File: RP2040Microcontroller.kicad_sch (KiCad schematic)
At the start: 128 parts, among them J2 Conn_01x02, J34 DIN-5_180degree, J36 USB_B, SW51 SW_Push, SW52 SW_Push, SW53 SW_Push, SW54 SW_Push, SW55 SW_Push, SW56 SW_Push, SW57 SW_Push, SW58 SW_Push, U1 NCP1117-3.3_SOT223, U2 W25Q128JVS, U3 RP2040, U39 CD74HC4067SM, U40 6N138, U43 TL074, U45 REF3012, U46 MCP4728, U47 TL074, U49 MCP23017_SS, Y1 ABLS-12.000MHZ-B4-T

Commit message: more work...
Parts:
- added J2: Conn_01x02, Connector_PinHeader_2.54mm:PinHeader_1x02_P2.54mm_Vertical, symbol Connector_Generic:Conn_01x02
- C1, C17, C4: value 10u -> 10uF
- C10, C8: value 1u -> 1uF; footprint Capacitor_SMD:C_0402_1005Metric -> Capacitor_SMD:C_0805_2012Metric
- C11, C12, C13, C14, C15, C16, C5, C6, C7, C9: value 100n -> 100nF; footprint Capacitor_SMD:C_0402_1005Metric -> Capacitor_SMD:C_0603_1608Metric
- C2, C3: value 27p -> 27pF; footprint Capacitor_SMD:C_0402_1005Metric -> Capacitor_SMD:C_0603_1608Metric
- C45: footprint Capacitor_SMD:C_0805_2012Metric_Pad1.18x1.45mm_HandSolder -> Capacitor_SMD:C_0603_1608Metric
- J34: value DIN-5_180degree -> DIN-504D-M5; footprint (none) -> SynthProjConnectors:SD-50BV
- J36: footprint (none) -> Connector_USB:USB_B_Lumberg_2411_02_Horizontal
- R1, R3, R4, R5: footprint Capacitor_SMD:C_0402_1005Metric -> Resistor_SMD:R_0603_1608Metric
- R? (x37): footprint Resistor_SMD:R_0805_2012Metric -> Resistor_SMD:R_0603_1608Metric
- R? (x17): footprint Resistor_SMD:R_0805_2012Metric_Pad1.20x1.40mm_HandSolder -> Resistor_SMD:R_0603_1608Metric
- U40: footprint (none) -> Package_SO:SOP-8_6.605x9.655mm_P2.54mm
- U43, U47: footprint (none) -> Package_SO:SO-14_3.9x8.65mm_P1.27mm
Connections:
- net GPIO0: now also J2.1 (Pin_1)
- net GPIO1: now also J2.2 (Pin_2)
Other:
- note added: "Debug"
- note added: "Voltage References"
- moved on the sheet: C2, C3, R5, R?, U43E, U45, Y1

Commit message: finishing schematic 1.0
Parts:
- added TP? (x6): TestPoint, TestPoint:TestPoint_Pad_D1.0mm, symbol Connector:TestPoint
- SW51, SW52, SW53, SW54, SW55, SW56, SW57, SW58: footprint (none) -> Button_Switch_THT:SW_PUSH_6mm_H13mm
- renumbered C15 to C?, C11 to C?, C13 to C?, C16 to C?, C14 to C?, C4 to C?, C2 to C?, C45 to C?, C3 to C?, C8 to C?, C7 to C?, C12 to C?, C9 to C?, C17 to C?, C6 to C?, C10 to C?, C1 to C?, C5 to C?, D10 to D?, J34 to J41, J36 to J42, J2 to J?, R2 to R?, R1 to R?, R3 to R?, R5 to R?, R4 to R?, RV39 to RV?, U49 to U44, U43 to U47, U47 to U49, U43 to U49, U2 to U?, U39 to U?, U3 to U?, U1 to U?, Y1 to Y?
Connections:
- net GPIO29_ADC0: now also TP?.1
- net VIN_A: now also TP?.1
- net VOUT_A: now also TP?.1
- net VREF1.0: now also TP?.1
- net VREF1.25: now also TP?.1
- net at C?.2, U46.6 (VOUTA): now also TP?.1
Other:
- moved on the sheet: C?, D?, J41, J42, J?, R?, RV?, SW51, SW52, SW53, SW54, SW55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

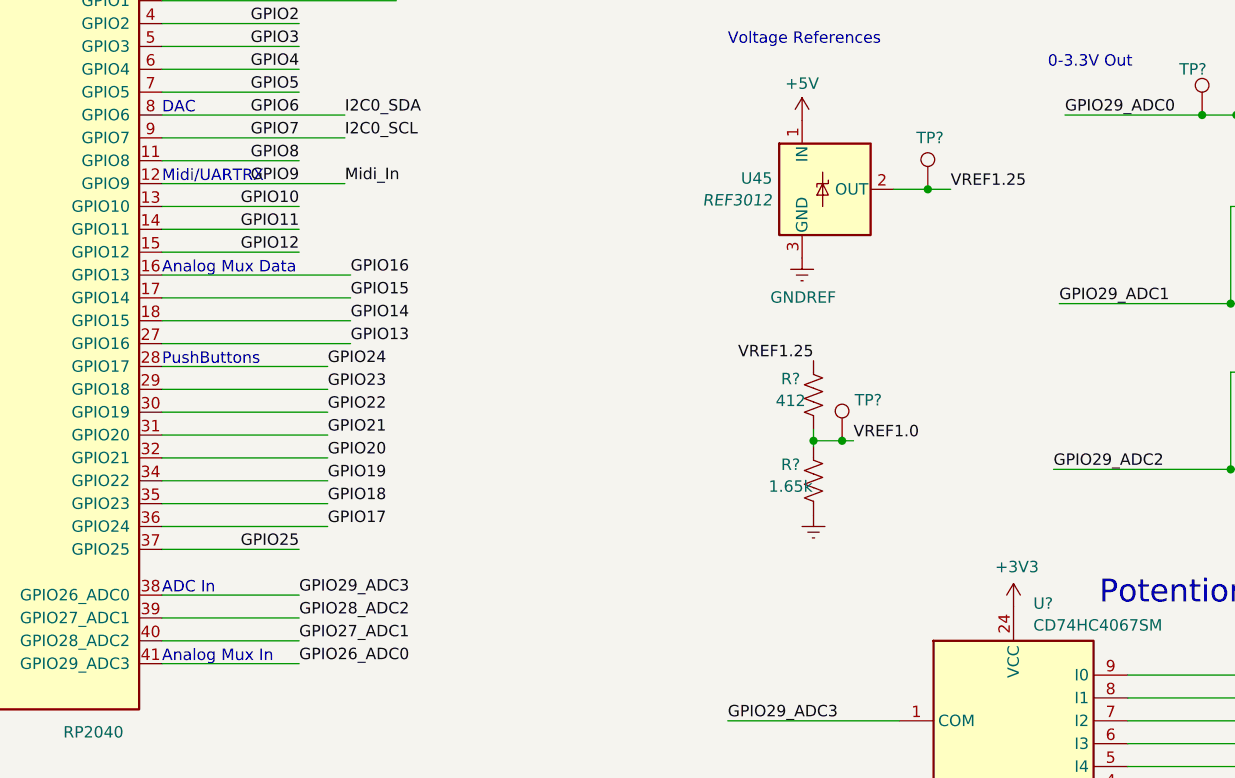
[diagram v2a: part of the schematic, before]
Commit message: doing some routing - split sequencer into another project
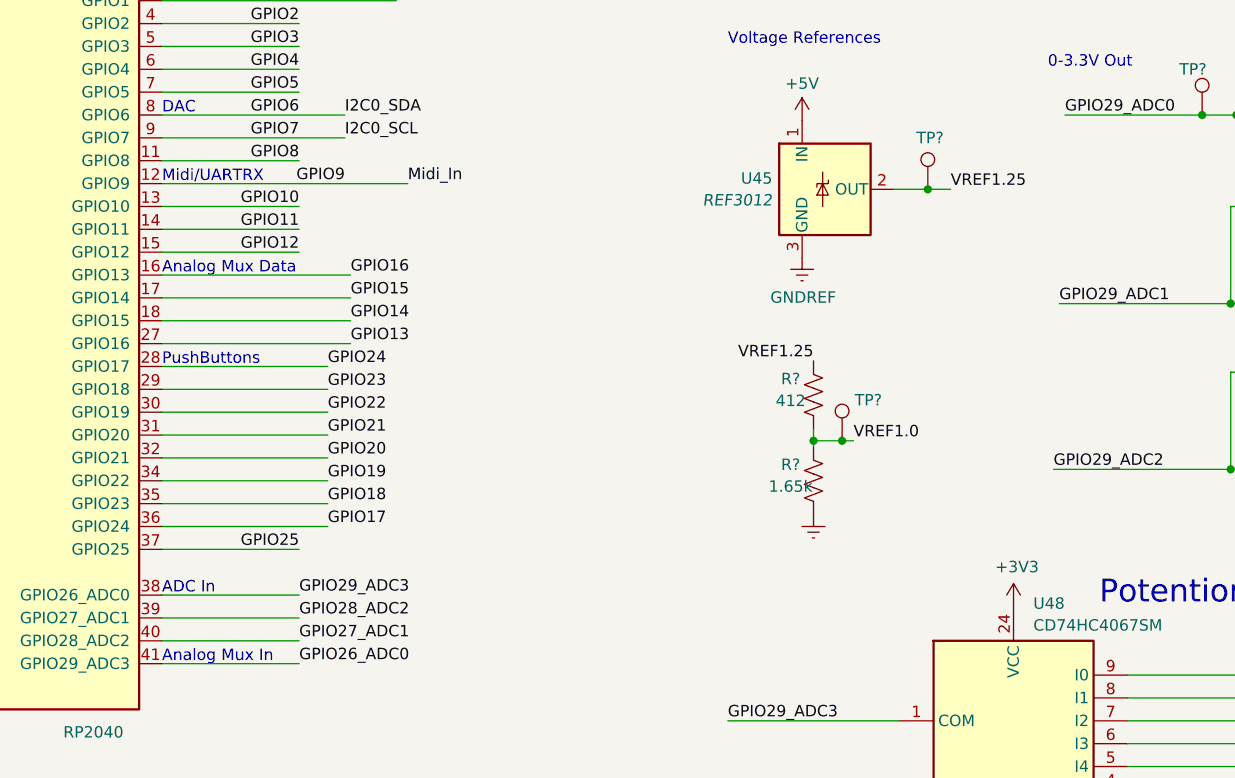
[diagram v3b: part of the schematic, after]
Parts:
- gave numbers to parts that had none: 1

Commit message: routing work...
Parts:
- removed R?: 28.7k, Resistor_SMD:R_0603_1608Metric, symbol Device:R_US
- removed R?: 10k, Resistor_SMD:R_0603_1608Metric, symbol Device:R_US
- removed R?: 66.5k, Resistor_SMD:R_0603_1608Metric, symbol Device:R_US
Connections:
- net VREF1.0: no longer U49.12 (+)
- net at U49.14: no longer U48.9 (I0)
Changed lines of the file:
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@@
 (kicad_sch (version 20230121) (generator eeschema)
   (paper "A3")
-  (junction (at 386.08 170.815) (diameter 0) (color 0 0 0 0)
-  )
   (junction (at 271.145 254) (diameter 0) (color 0 0 0 0)
   )
   (junction (at 88.9 94.615) (diameter 0) (color 0 0 0 0)
   )
-  (junction (at 368.3 181.61) (diameter 0) (color 0 0 0 0)
-  )
   (junction (at 207.645 73.66) (diameter 0) (color 0 0 0 0)
   )
@@
   (junction (at 368.3 41.275) (diameter 0) (color 0 0 0 0)
   )
-  (junction (at 386.08 179.07) (diameter 0) (color 0 0 0 0)
-  )
   (junction (at 271.145 231.14) (diameter 0) (color 0 0 0 0)
   )
@@
     (stroke (width 0) (type default))
   )
-  (wire (pts (xy 386.08 179.07) (xy 384.81 179.07))
-    (stroke (width 0) (type default))
-  )
   (wire (pts (xy 153.67 229.87) (xy 156.845 229.87))
     (stroke (width 0) (type default))
@@
     (stroke (width 0) (type default))
   )
-  (wire (pts (xy 386.08 170.815) (xy 378.46 170.815))
-    (stroke (width 0) (type default))
-  )
   (wire (pts (xy 351.79 212.09) (xy 377.19 212.09))
     (stroke (width 0) (type default))
@@
     (stroke (width 0) (type default))
   )
-  (wire (pts (xy 396.875 184.15) (xy 384.81 184.15))
-    (stroke (width 0) (type default))
-  )
   (wire (pts (xy 273.685 54.61) (xy 273.685 53.34))
     (stroke (width 0) (type default))
@@
     (stroke (width 0) (type default))
   )
-  (wire (pts (xy 397.51 179.07) (xy 396.875 179.07))
-    (stroke (width 0) (type default))
-  )
   (wire (pts (xy 342.265 119.38) (xy 343.535 119.38))
     (stroke (width 0) (type default))
@@
     (stroke (width 0) (type default))
   )
-  (wire (pts (xy 330.2 181.61) (xy 368.3 181.61))
-    (stroke (width 0) (type default))
-  )
   (wire (pts (xy 182.245 86.36) (xy 182.245 73.66))
     (stroke (width 0) (type default))
@@
     (stroke (width 0) (type default))
   )
-  (wire (pts (xy 389.255 179.07) (xy 386.08 179.07))
-    (stroke (width 0) (type default))
-  )
   (wire (pts (xy 321.945 158.75) (xy 341.63 158.75))
     (stroke (width 0) (type default))
@@
     (stroke (width 0) (type default))
   )
-  (wire (pts (xy 368.3 181.61) (xy 369.57 181.61))
-    (stroke (width 0) (type default))
-  )
   (wire (pts (xy 170.815 73.66) (xy 170.815 86.36))
     (stroke (width 0) (type default))
@@
     (stroke (width 0) (type default))
   )
-  (wire (pts (xy 368.3 170.815) (xy 368.3 181.61))
-    (stroke (width 0) (type default))
-  )
   (wire (pts (xy 67.31 209.55) (xy 67.31 214.63))
     (stroke (width 0) (type default))
@@
     (stroke (width 0) (type default))
   )
-  (wire (pts (xy 386.08 179.07) (xy 386.08 170.815))
-    (stroke (width 0) (type default))
-  )
   (wire (pts (xy 295.275 155.575) (xy 298.45 155.575))
     (stroke (width 0) (type default))
@@
     (stroke (width 0) (type default))
   )
-  (wire (pts (xy 370.84 170.815) (xy 368.3 170.815))
-    (stroke (width 0) (type default))
-  )
   (wire (pts (xy 159.385 171.45) (xy 145.415 171.45))
     (stroke (width 0) (type default))
@@
     (stroke (width 0) (type default))
   )
-  (wire (pts (xy 389.89 170.815) (xy 386.08 170.815))
-    (stroke (width 0) (type default))
-  )
   (wire (pts (xy 307.975 127.635) (xy 310.515 127.635))
     (stroke (width 0) (type default))
@@
     (effects (font (size 1.27 1.27)) (justify left bottom))
   )
-  (label "VREF1.0" (at 396.875 184.15 0) (fields_autoplaced)
-    (effects (font (size 1.27 1.27)) (justify left bottom))
-  )
   (label "QSPI_SD1" (at 118.11 114.935 180) (fields_autoplaced)
     (effects (font (size 1.27 1.27)) (justify right bottom))
@@
     (effects (font (size 1.27 1.27)) (justify left))
   )
-  (hierarchical_label "VIN_D" (shape input) (at 397.51 179.07 0) (fields_autoplaced)
-    (effects (font (size 1.27 1.27)) (justify left))
-  )
   (hierarchical_label "VIN_C" (shape input) (at 374.65 156.21 0) (fields_autoplaced)
     (effects (font (size 1.27 1.27)) (justify left))
@@
     )
   )
-  (symbol (lib_id "power:GNDREF") (at 397.51 170.815 0) (mirror y) (unit 1)
-    (in_bom yes) (on_board yes) (dnp no)
-    (property "Reference" "#PWR?" (at 397.51 177.165 0)
-      (effects (font (size 1.27 1.27)) hide)
-    )
-    (property "Value" "GNDREF" (at 397.383 175.2092 0)
-      (effects (font (size 1.27 1.27)) hide)
-    )
-    (property "Footprint" "" (at 397.51 170.815 0)
-      (effects (font (size 1.27 1.27)) hide)
-    )
-    (property "Datasheet" "" (at 397.51 170.815 0)
-      (effects (font (size 1.27 1.27)) hide)
-    )
-    (pin "1")
-    (instances
-      (project "SynthProj"
-        (path "/9021c97e-351f-4ed9-b393-50257df6a463/00000000-0000-0000-0000-0000659d0967"
-          (reference "#PWR?") (unit 1)
-        )
-        (path "/9021c97e-351f-4ed9-b393-50257df6a463/00000000-0000-0000-0000-0000659a4e2e"
-          (reference "#PWR?") (unit 1)
-        )
-        (path "/9021c97e-351f-4ed9-b393-50257df6a463/2f8f79cd-08c7-4a3d-ab4d-798613b0e4e6"
-          (reference "#PWR0524") (unit 1)
-        )
-      )
-    )
-  )
   (symbol (lib_id "Device:R_US") (at 367.03 129.54 90) (unit 1)
     (in_bom yes) (on_board yes) (dnp no)
@@
     )
   )
-  (symbol (lib_id "Device:R_US") (at 393.7 170.815 90) (unit 1)
-    (in_bom yes) (on_board yes) (dnp no)
-    (property "Reference" "R?" (at 393.7 168.275 90)
-      (effects (font (size 1.27 1.27)))
-    )
-    (property "Value" "28.7k" (at 393.7 165.735 90)
-      (effects (font (size 1.27 1.27)))
-    )
-    (property "Footprint" "Resistor_SMD:R_0603_1608Metric" (at 393.954 169.799 90)
-      (effects (font (size 1.27 1.27)) hide)
-    )
-    (property "Datasheet" "~" (at 393.7 170.815 0)
-      (effects (font (size 1.27 1.27)) hide)
-    )
-    (pin "2")
-    (pin "1")
-    (instances
-      (project "SynthProj"
-        (path "/9021c97e-351f-4ed9-b393-50257df6a463/00000000-0000-0000-0000-0000659d0967"
-          (reference "R?") (unit 1)
-        )
-        (path "/9021c97e-351f-4ed9-b393-50257df6a463/00000000-0000-0000-0000-0000659a4e2e"
-          (reference "R?") (unit 1)
-        )
-        (path "/9021c97e-351f-4ed9-b393-50257df6a463/0e948a88-c071-4754-aa3e-af223f738530"
-          (reference "R?") (unit 1)
-        )
-        (path "/9021c97e-351f-4ed9-b393-50257df6a463/2f8f79cd-08c7-4a3d-ab4d-798613b0e4e6"
-          (reference "R404") (unit 1)
-        )
-      )
-    )
-  )
   (symbol (lib_id "power:+3V3") (at 373.38 200.66 90) (unit 1)
     (in_bom yes) (on_board yes) (dnp no)
@@
     )
   )
-  (symbol (lib_id "Device:R_US") (at 374.65 170.815 90) (unit 1)
-    (in_bom yes) (on_board yes) (dnp no)
-    (property "Reference" "R?" (at 370.84 169.545 90)
-      (effects (font (size 1.27 1.27)))
-    )
-    (property "Value" "10k" (at 370.84 172.085 90)
-      (effects (font (size 1.27 1.27)))
-    )
-    (property "Footprint" "Resistor_SMD:R_0603_1608Metric" (at 374.904 169.799 90)
-      (effects (font (size 1.27 1.27)) hide)
-    )
-    (property "Datasheet" "~" (at 374.65 170.815 0)
-      (effects (font (size 1.27 1.27)) hide)
-    )
-    (pin "2")
-    (pin "1")
-    (instances
-      (project "SynthProj"
-        (path "/9021c97e-351f-4ed9-b393-50257df6a463/00000000-0000-0000-0000-0000659d0967"
-          (reference "R?") (unit 1)
-        )
-        (path "/9021c97e-351f-4ed9-b393-50257df6a463/00000000-0000-0000-0000-0000659a4e2e"
-          (reference "R?") (unit 1)
-        )
-        (path "/9021c97e-351f-4ed9-b393-50257df6a463/0e948a88-c071-4754-aa3e-af223f738530"
-          (reference "R?") (unit 1)
-        )
-        (path "/9021c97e-351f-4ed9-b393-50257df6a463/2f8f79cd-08c7-4a3d-ab4d-798613b0e4e6"
-          (reference "R402") (unit 1)
-        )
-      )
-    )
-  )
   (symbol (lib_id "power:GNDD") (at 161.925 78.74 0) (unit 1)
     (in_bom yes) (on_board yes) (dnp no) (fields_autoplaced)
@@
         )
       )
-    )
-  )
-  (symbol (lib_id "Device:R_US") (at 393.065 179.07 90) (unit 1)
-    (in_bom yes) (on_board yes) (dnp no)
-    (property "Reference" "R?" (at 393.065 176.53 90)
-      (effects (font (size 1.27 1.27)))
-    )
-    (property "Value" "66.5k" (at 393.065 173.99 90)
-      (effects (font (size 1.27 1.27)))
-    )
-    (property "Footprint" "Resistor_SMD:R_0603_1608Metric" (at 393.319 178.054 90)
-      (effects (font (size 1.27 1.27)) hide)
-    )
-    (property "Datasheet" "~" (at 393.065 179.07 0)
-      (effects (font (size 1.27 1.27)) hide)
-    )
-    (pin "2")
-    (pin "1")
-    (instances
-      (project "SynthProj"
-        (path "/9021c97e-351f-4ed9-b393-50257df6a463/00000000-0000-0000-0000-0000659d0967"
-          (reference "R?") (unit 1)
-        )
-        (path "/9021c97e-351f-4ed9-b393-50257df6a463/00000000-0000-0000-0000-0000659a4e2e"
-          (reference "R?") (unit 1)
-        )
-        (path "/9021c97e-351f-4ed9-b393-50257df6a463/0e948a88-c071-4754-aa3e-af223f738530"
-          (reference "R?") (unit 1)
-        )
-        (path "/9021c97e-351f-4ed9-b393-50257df6a463/2f8f79cd-08c7-4a3d-ab4d-798613b0e4e6"
-          (reference "R403") (unit 1)
-        )
-      )

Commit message: routing work...
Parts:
- added J5: Conn_01x18, symbol Connector_Generic:Conn_01x18
- J42: footprint Connector_USB:USB_B_Lumberg_2411_02_Horizontal -> Connector_USB:USB_B_TE_5787834_Vertical
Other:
- note added: "EYESPI Display Connector"
- moved on the sheet: C?, D?, J41, J?, R?, SW51, SW52, SW53, SW54, SW55, SW56, SW57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

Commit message: routing... placing... going cross eyed...
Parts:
- removed R? (x6): 100k, Resistor_SMD:R_0603_1608Metric, symbol Device:R_US
- removed RV? (x8): 100k, Potentiometer_THT:Potentiometer_Alps_RK09K_Single_Vertical, symbol SynthProj-rescue:R_POT_US-Device
- removed SW51, SW52, SW53, SW54, SW55, SW57: SW_Push, Button_Switch_THT:SW_PUSH_6mm_H13mm, symbol Switch:SW_Push
- added J15: Micro_SD_Card, symbol Connector:Micro_SD_Card
- added RV? (x3): 100k, Potentiometer_THT:Potentiometer_Alps_RK09K_Single_Vertical, symbol SynthProj-rescue:R_POT_US-Device
- J5: footprint (none) -> Connector_FFC-FPC:Hirose_FH12-18S-0.5SH_1x18-1MP_P0.50mm_Horizontal
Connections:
- net +3V3: now also RV?.3, RV?.3, RV?.3
- net GNDREF: now also RV?.1, RV?.1, RV?.1
- net at U48.7 (I2): now also RV?.2
- net at U48.6 (I3): now also RV?.2
- net at U48.8 (I1): now also RV?.2
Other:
- note added: "BUSY"
- note added: "CARDCS"
- note added: "GND"
- note added: "GPIO1"
- note added: "INT"
- note added: "LITE"
- note added: "MEM_CS"
- note added: "MISO"
- note added: "MOSI"
- note added: "SCK"
- note added: "SCL"
- note added: "SDA"
- note added: "TFTCS"
- note added: "TFTDC"
- note added: "TFTRST"
- note added: "TSCS"
- note added: "VCC"
- moved on the sheet: C?, D?, J41, J42, J?, R?, SW56, SW58, U40, U?, Y?

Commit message: more work
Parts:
- D? (x16): footprint LED_SMD:LED_0805_2012Metric -> LED_THT:LED_D3.0mm
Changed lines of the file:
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@@
       (effects (font (size 1.27 1.27)) (justify left) hide)
     )
-    (property "Footprint" "LED_SMD:LED_0805_2012Metric" (at 253.365 213.36 0)
+    (property "Footprint" "LED_THT:LED_D3.0mm" (at 253.365 213.36 0)
       (effects (font (size 1.27 1.27)) hide)
     )
@@
       (effects (font (size 1.27 1.27)) (justify left) hide)
     )
-    (property "Footprint" "LED_SMD:LED_0805_2012Metric" (at 253.365 246.38 0)
+    (property "Footprint" "LED_THT:LED_D3.0mm" (at 253.365 246.38 0)
       (effects (font (size 1.27 1.27)) hide)
     )
@@
       (effects (font (size 1.27 1.27)) (justify left) hide)
     )
-    (property "Footprint" "LED_SMD:LED_0805_2012Metric" (at 253.365 238.76 0)
+    (property "Footprint" "LED_THT:LED_D3.0mm" (at 253.365 238.76 0)
       (effects (font (size 1.27 1.27)) hide)
     )
@@
       (effects (font (size 1.27 1.27)) (justify left) hide)
     )
-    (property "Footprint" "LED_SMD:LED_0805_2012Metric" (at 253.365 215.9 0)
+    (property "Footprint" "LED_THT:LED_D3.0mm" (at 253.365 215.9 0)
       (effects (font (size 1.27 1.27)) hide)
     )
@@
       (effects (font (size 1.27 1.27)) (justify left) hide)
     )
-    (property "Footprint" "LED_SMD:LED_0805_2012Metric" (at 253.365 223.52 0)
+    (property "Footprint" "LED_THT:LED_D3.0mm" (at 253.365 223.52 0)
       (effects (font (size 1.27 1.27)) hide)
     )
@@
       (effects (font (size 1.27 1.27)) (justify left) hide)
     )
-    (property "Footprint" "LED_SMD:LED_0805_2012Metric" (at 253.365 220.98 0)
+    (property "Footprint" "LED_THT:LED_D3.0mm" (at 253.365 220.98 0)
       (effects (font (size 1.27 1.27)) hide)
     )
@@
       (effects (font (size 1.27 1.27)) (justify left) hide)
     )
-    (property "Footprint" "LED_SMD:LED_0805_2012Metric" (at 253.365 226.06 0)
+    (property "Footprint" "LED_THT:LED_D3.0mm" (at 253.365 226.06 0)
       (effects (font (size 1.27 1.27)) hide)
     )
@@
       (effects (font (size 1.27 1.27)) (justify left) hide)
     )
-    (property "Footprint" "LED_SMD:LED_0805_2012Metric" (at 253.365 236.22 0)
+    (property "Footprint" "LED_THT:LED_D3.0mm" (at 253.365 236.22 0)
       (effects (font (size 1.27 1.27)) hide)
     )
@@
       (effects (font (size 1.27 1.27)) (justify left) hide)
     )
-    (property "Footprint" "LED_SMD:LED_0805_2012Metric" (at 253.365 251.46 0)
+    (property "Footprint" "LED_THT:LED_D3.0mm" (at 253.365 251.46 0)
       (effects (font (size 1.27 1.27)) hide)
     )
@@
       (effects (font (size 1.27 1.27)) (justify left) hide)
     )
-    (property "Footprint" "LED_SMD:LED_0805_2012Metric" (at 253.365 243.84 0)
+    (property "Footprint" "LED_THT:LED_D3.0mm" (at 253.365 243.84 0)
       (effects (font (size 1.27 1.27)) hide)
     )
@@
       (effects (font (size 1.27 1.27)) (justify left) hide)
     )
-    (property "Footprint" "LED_SMD:LED_0805_2012Metric" (at 253.365 241.3 0)
+    (property "Footprint" "LED_THT:LED_D3.0mm" (at 253.365 241.3 0)
       (effects (font (size 1.27 1.27)) hide)
     )
@@
       (effects (font (size 1.27 1.27)) (justify left) hide)
     )
-    (property "Footprint" "LED_SMD:LED_0805_2012Metric" (at 253.365 218.44 0)
+    (property "Footprint" "LED_THT:LED_D3.0mm" (at 253.365 218.44 0)
       (effects (font (size 1.27 1.27)) hide)
     )
@@
       (effects (font (size 1.27 1.27)) (justify left) hide)
     )
-    (property "Footprint" "LED_SMD:LED_0805_2012Metric" (at 253.365 228.6 0)
+    (property "Footprint" "LED_THT:LED_D3.0mm" (at 253.365 228.6 0)
       (effects (font (size 1.27 1.27)) hide)
     )
@@
       (effects (font (size 1.27 1.27)) (justify left) hide)
     )
-    (property "Footprint" "LED_SMD:LED_0805_2012Metric" (at 253.365 233.68 0)
+    (property "Footprint" "LED_THT:LED_D3.0mm" (at 253.365 233.68 0)
       (effects (font (size 1.27 1.27)) hide)
     )
@@
       (effects (font (size 1.27 1.27)) (justify left) hide)
     )
-    (property "Footprint" "LED_SMD:LED_0805_2012Metric" (at 253.365 210.82 0)
+    (property "Footprint" "LED_THT:LED_D3.0mm" (at 253.365 210.82 0)
       (effects (font (size 1.27 1.27)) hide)
     )
@@
       (effects (font (size 1.27 1.27)) (justify left) hide)
     )
-    (property "Footprint" "LED_SMD:LED_0805_2012Metric" (at 253.365 248.92 0)
+    (property "Footprint" "LED_THT:LED_D3.0mm" (at 253.365 248.92 0)
       (effects (font (size 1.27 1.27)) hide)
     )
